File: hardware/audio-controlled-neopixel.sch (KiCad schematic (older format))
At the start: 63 parts, among them J1 AudioJack4, J2 AudioJack4, J3 KF2EDGK, J4 KF2EDGK, J5 KF2EDGK, J6 Conn_01x01_Female, J7 Conn_01x01_Female, J8 Conn_01x01_Female, J9 Conn_01x01_Female, SW1 SW_SPST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

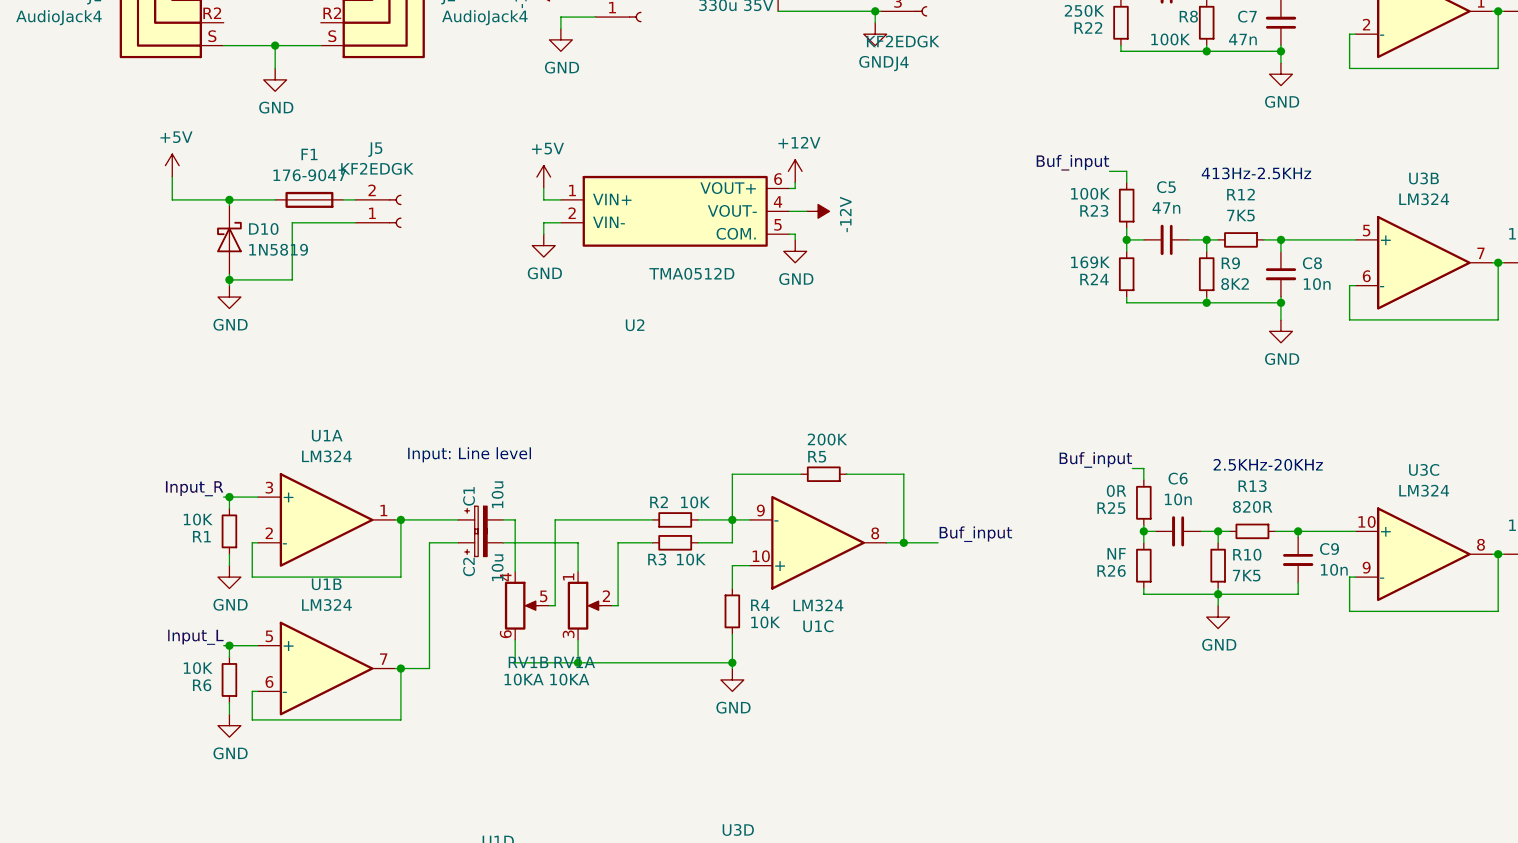
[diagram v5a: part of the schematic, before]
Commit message: Added input resistors
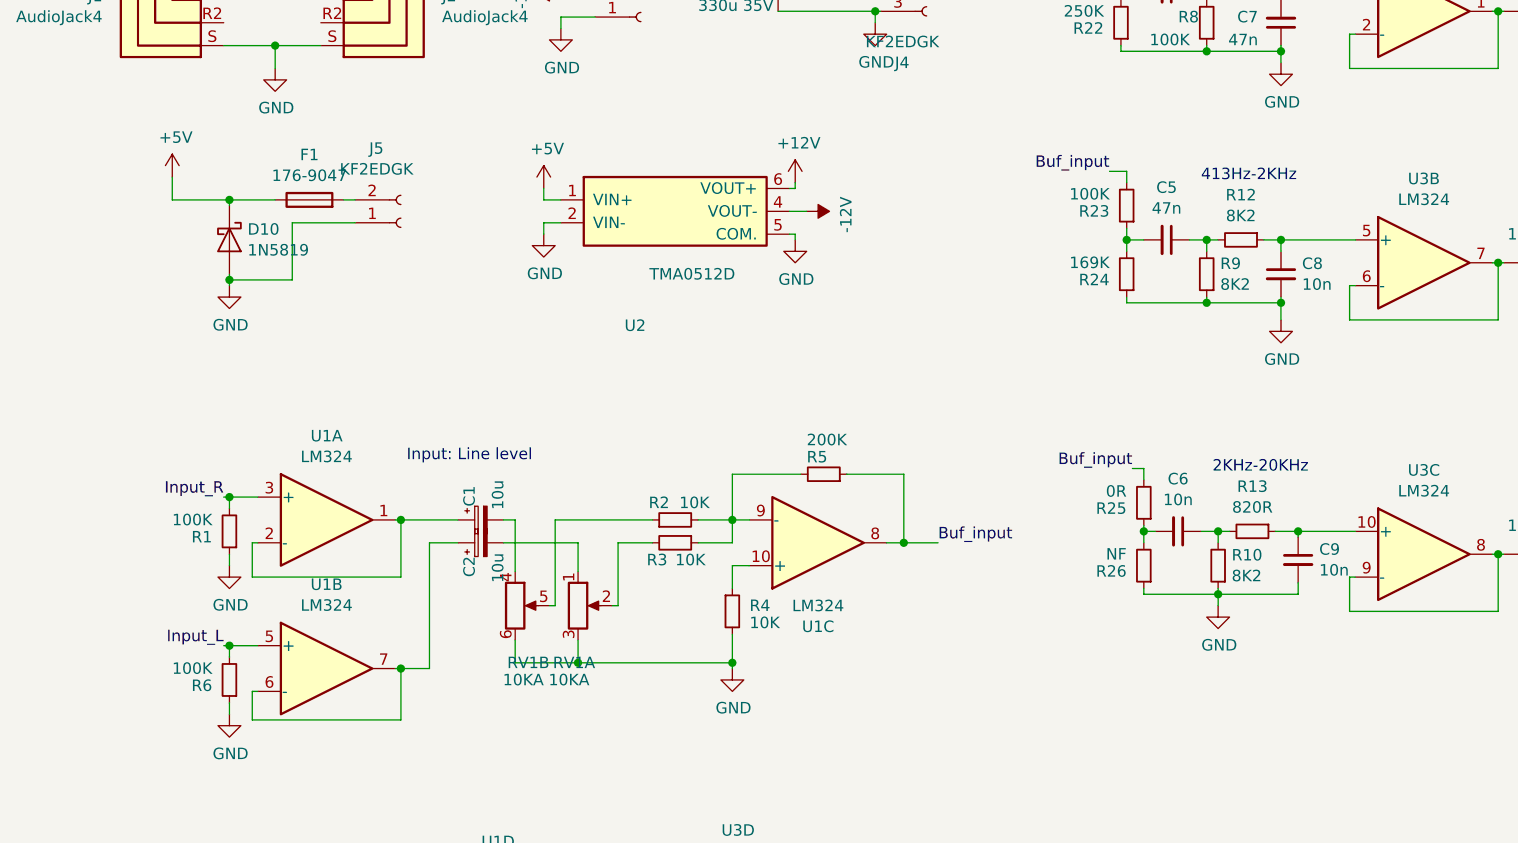
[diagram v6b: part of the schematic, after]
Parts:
- R1, R6: value 10K -> 100K
- R10, R12: value 7K5 -> 8K2
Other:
- note added: "2KHz-20KHz"
- note added: "413Hz-2KHz"
- note removed: "2.5KHz-20KHz"
- note removed: "413Hz-2.5KHz"
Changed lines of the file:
@@
 P 5425 2050
 F 0 "R12" V 5229 2050 50  0000 C CNN
-F 1 "7K5" V 5320 2050 50  0000 C CNN
+F 1 "8K2" V 5320 2050 50  0000 C CNN
 F 2 "Resistor_SMD:R_0805_2012Metric" H 5425 2050 50  0001 C CNN
 F 3 "~" H 5425 2050 50  0001 C CNN
@@
 P 5325 3475
 F 0 "R10" H 5266 3429 50  0000 R CNN
-F 1 "7K5" H 5266 3520 50  0000 R CNN
+F 1 "8K2" H 5266 3520 50  0000 R CNN
 F 2 "Resistor_SMD:R_0805_2012Metric" H 5325 3475 50  0001 C CNN
 F 3 "~" H 5325 3475 50  0001 C CNN
@@
 16-413Hz
 Text Notes 5250 1800 0    50   ~ 0
-413Hz-2.5KHz
+413Hz-2KHz
 Text Notes 5300 3075 0    50   ~ 0
-2.5KHz-20KHz
+2KHz-20KHz
 Connection ~ 7225 2150
 $Comp
@@
 P 1000 3975
 F 0 "R6" H 1075 4000 50  0000 L CNN
-F 1 "10K" H 1075 3925 50  0000 L CNN
+F 1 "100K" H 1075 3925 50  0000 L CNN
 F 2 "Resistor_SMD:R_0805_2012Metric" H 1000 3975 50  0001 C CNN
 F 3 "~" H 1000 3975 50  0001 C CNN
@@
 P 1000 3325
 F 0 "R1" H 1075 3350 50  0000 L CNN
-F 1 "10K" H 1075 3275 50  0000 L CNN
+F 1 "100K" H 1075 3275 50  0000 L CNN
 F 2 "Resistor_SMD:R_0805_2012Metric" H 1000 3325 50  0001 C CNN
 F 3 "~" H 1000 3325 50  0001 C CNN

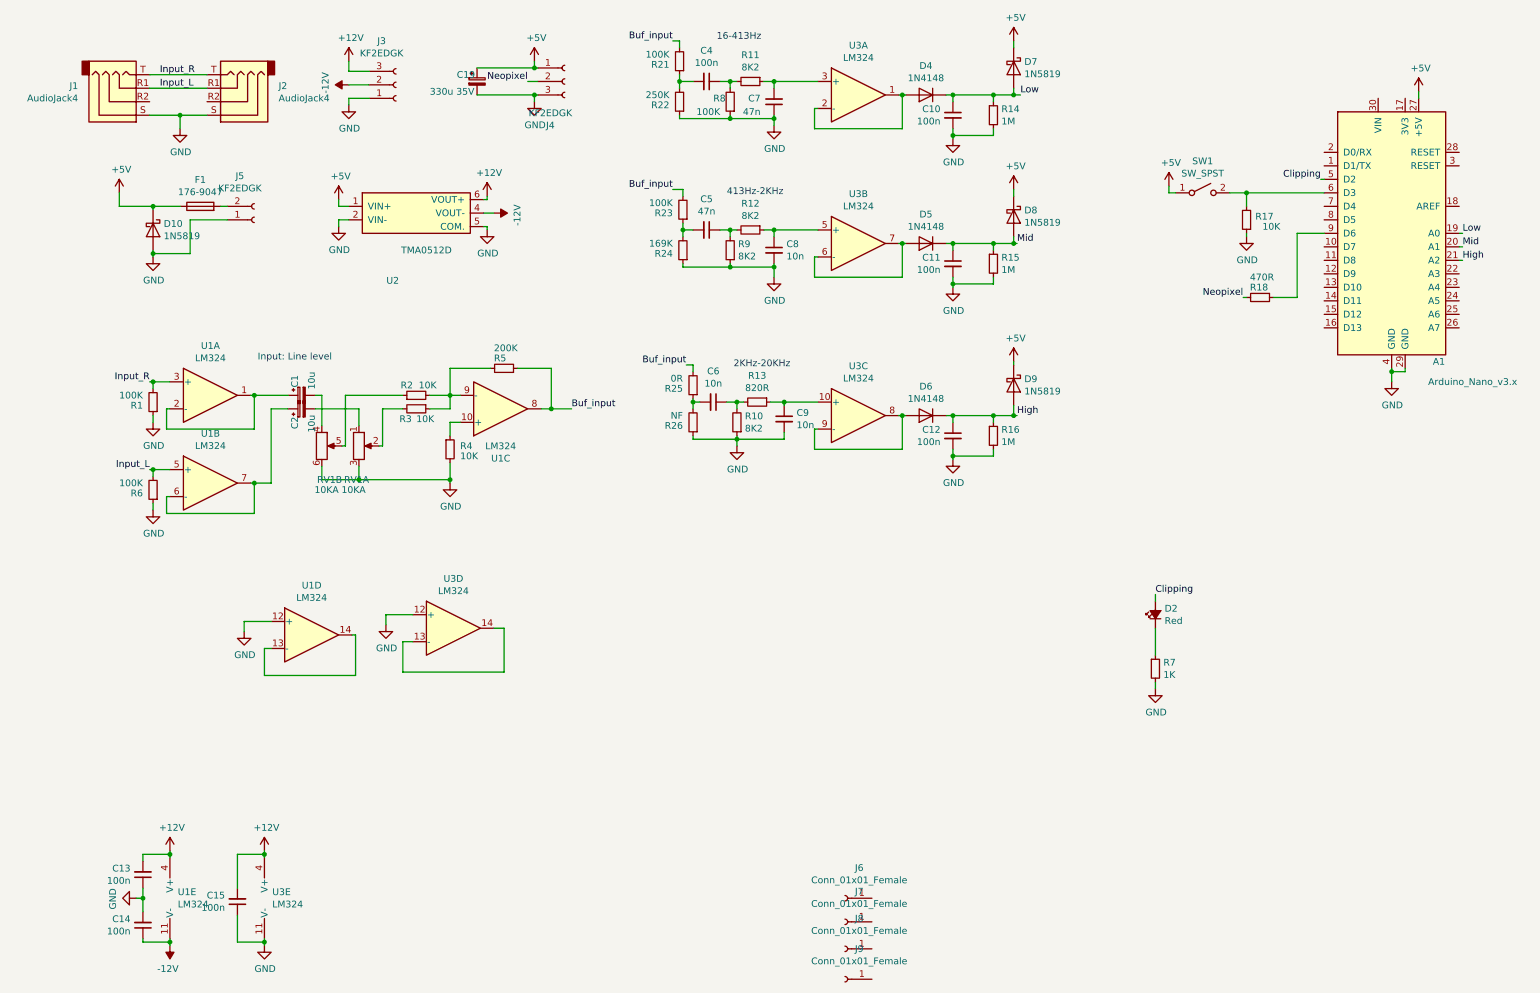
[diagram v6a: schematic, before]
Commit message: Cleaned up schematic, refactored code for latest hardware
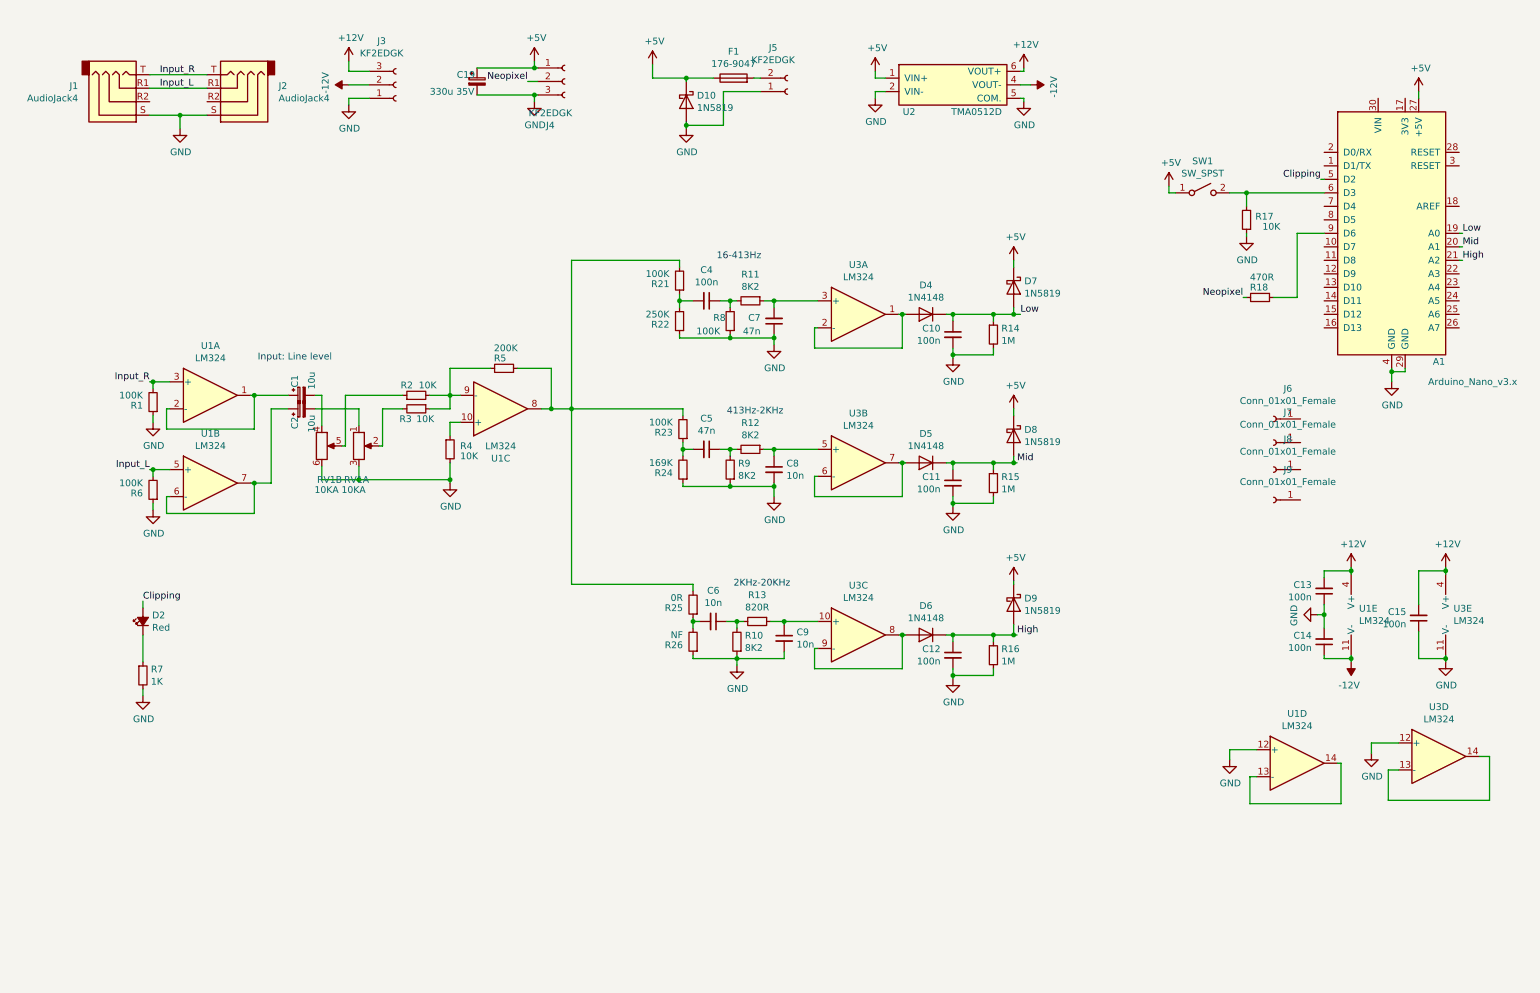
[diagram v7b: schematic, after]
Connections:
- net Buf_input: no longer names the net of R21.2, R23.2, R25.2, R5.1, U1.8
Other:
- moved on the sheet: C10, C11, C12, C13, C14, C15, C4, C5, C6, C7, C8, C9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

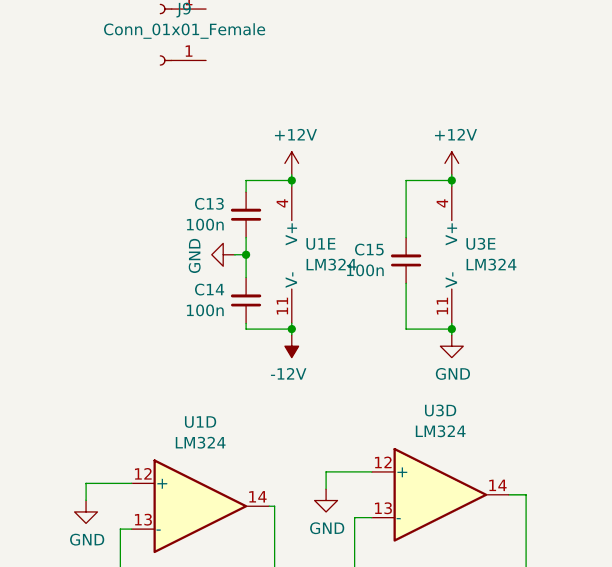
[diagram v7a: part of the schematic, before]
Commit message: connect both op-amps to dual supply
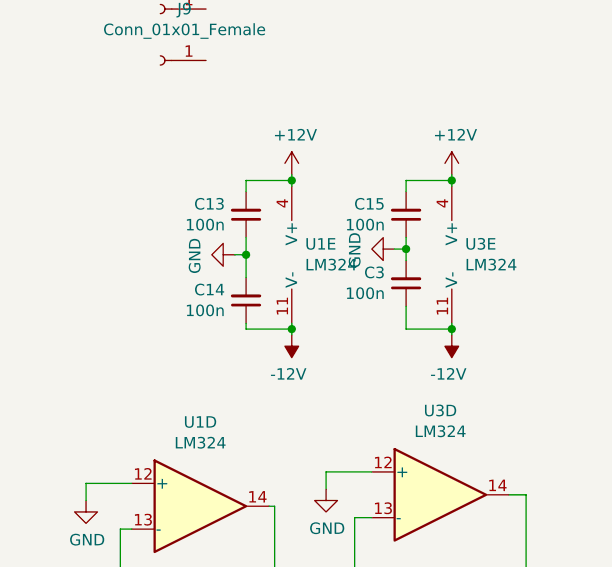
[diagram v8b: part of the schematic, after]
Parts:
- added C3: 100n, Capacitor_SMD:C_0805_2012Metric, symbol Device:C_Small
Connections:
- net -12V: now also U3.11 (V-), C3.1
- net GND: now also C3.2; no longer U3.11 (V-)
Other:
- moved on the sheet: C15
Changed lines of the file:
@@
 L Device:C_Small C15
 U 1 1 5BE11C86
-P 10375 4925
-F 0 "C15" H 10283 4879 50  0000 R CNN
-F 1 "100n" H 10283 4970 50  0000 R CNN
-F 2 "Capacitor_SMD:C_0805_2012Metric" H 10375 4925 50  0001 C CNN
-F 3 "~" H 10375 4925 50  0001 C CNN
-	1    10375 4925
+P 10375 4725
+F 0 "C15" H 10283 4679 50  0000 R CNN
+F 1 "100n" H 10283 4770 50  0000 R CNN
+F 2 "Capacitor_SMD:C_0805_2012Metric" H 10375 4725 50  0001 C CNN
+F 3 "~" H 10375 4725 50  0001 C CNN
+	1    10375 4725
 	1    0    0    1
 $EndComp
@@
 	10575 4550 10575 4575
 Connection ~ 10575 4575
-Wire Wire Line
-	10375 4575 10375 4825
 Text Notes 1775 3025 0    50   ~ 0
 Input: Line level
@@
 Connection ~ 1750 3925
 $Comp
-L power:GND #PWR02
-U 1 1 5BFD3352
-P 10575 5250
-F 0 "#PWR02" H 10575 5000 50  0001 C CNN
-F 1 "GND" H 10580 5077 50  0000 C CNN
-F 2 "" H 10575 5250 50  0001 C CNN
-F 3 "" H 10575 5250 50  0001 C CNN
-	1    10575 5250
-	1    0    0    -1
-$EndComp
-$Comp
 L Amplifier_Operational:LM324 U3
 U 1 1 5C09A93E
@@
 	-1   0    0    1
 $EndComp
-Wire Wire Line
-	10375 5025 10375 5225
 $Comp
 L Connector:AudioJack4 J1
@@
 Wire Wire Line
 	4100 2275 4900 2275
+$Comp
+L power:-12V #PWR0136
+U 1 1 5CB04C71
+P 10575 5250
+F 0 "#PWR0136" H 10575 5350 50  0001 C CNN
+F 1 "-12V" H 10590 5423 50  0000 C CNN
+F 2 "" H 10575 5250 50  0001 C CNN
+F 3 "" H 10575 5250 50  0001 C CNN
+	1    10575 5250
+	-1   0    0    1
+$EndComp
+$Comp
+L Device:C_Small C3
+U 1 1 5CB05249
+P 10375 5025
+F 0 "C3" H 10283 4979 50  0000 R CNN
+F 1 "100n" H 10283 5070 50  0000 R CNN
+F 2 "Capacitor_SMD:C_0805_2012Metric" H 10375 5025 50  0001 C CNN
+F 3 "~" H 10375 5025 50  0001 C CNN
+	1    10375 5025
+	1    0    0    1
+$EndComp
+Wire Wire Line
+	10375 4575 10375 4625
+Wire Wire Line
+	10375 4825 10375 4875
+Wire Wire Line
+	10375 5125 10375 5225
+$Comp
+L power:GND #PWR0137
+U 1 1 5CB39B64
+P 10325 4875
+F 0 "#PWR0137" H 10325 4625 50  0001 C CNN
+F 1 "GND" H 10330 4702 50  0000 C CNN
+F 2 "" H 10325 4875 50  0001 C CNN
+F 3 "" H 10325 4875 50  0001 C CNN
+	1    10325 4875
+	0    1    1    0
+$EndComp
+Wire Wire Line
+	10325 4875 10375 4875
+Connection ~ 10375 4875
+Wire Wire Line
+	10375 4875 10375 4925
 $EndSCHEMATC
